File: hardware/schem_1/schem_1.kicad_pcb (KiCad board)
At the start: 4 copper layers, 69.9 x 34 mm, 87 parts, among them J1 OV7670_Conn_01x24_MountingPin, J2 Micro_SD_Card, J3 FRONT_PCB_CONNECTOR, J4 BG300-04-X-X-A_REVC, J5 UJ2-MBH-1-SMT, J6 BACK_PCB_CONNECTOR, Q1 NDS332P, SW1 BTN_BOOT, SW2 ESP32_RESET, SW4 DOWN, SW5 UP, SW6 OK, U1 ESP32-WROVER-E-JC, U2 XC6210B332MR, U5 XC6206-2.8V, U6 XC6206-1.2V, U7 128x32_OLED_SSD1306, U8 MCP23017_SO

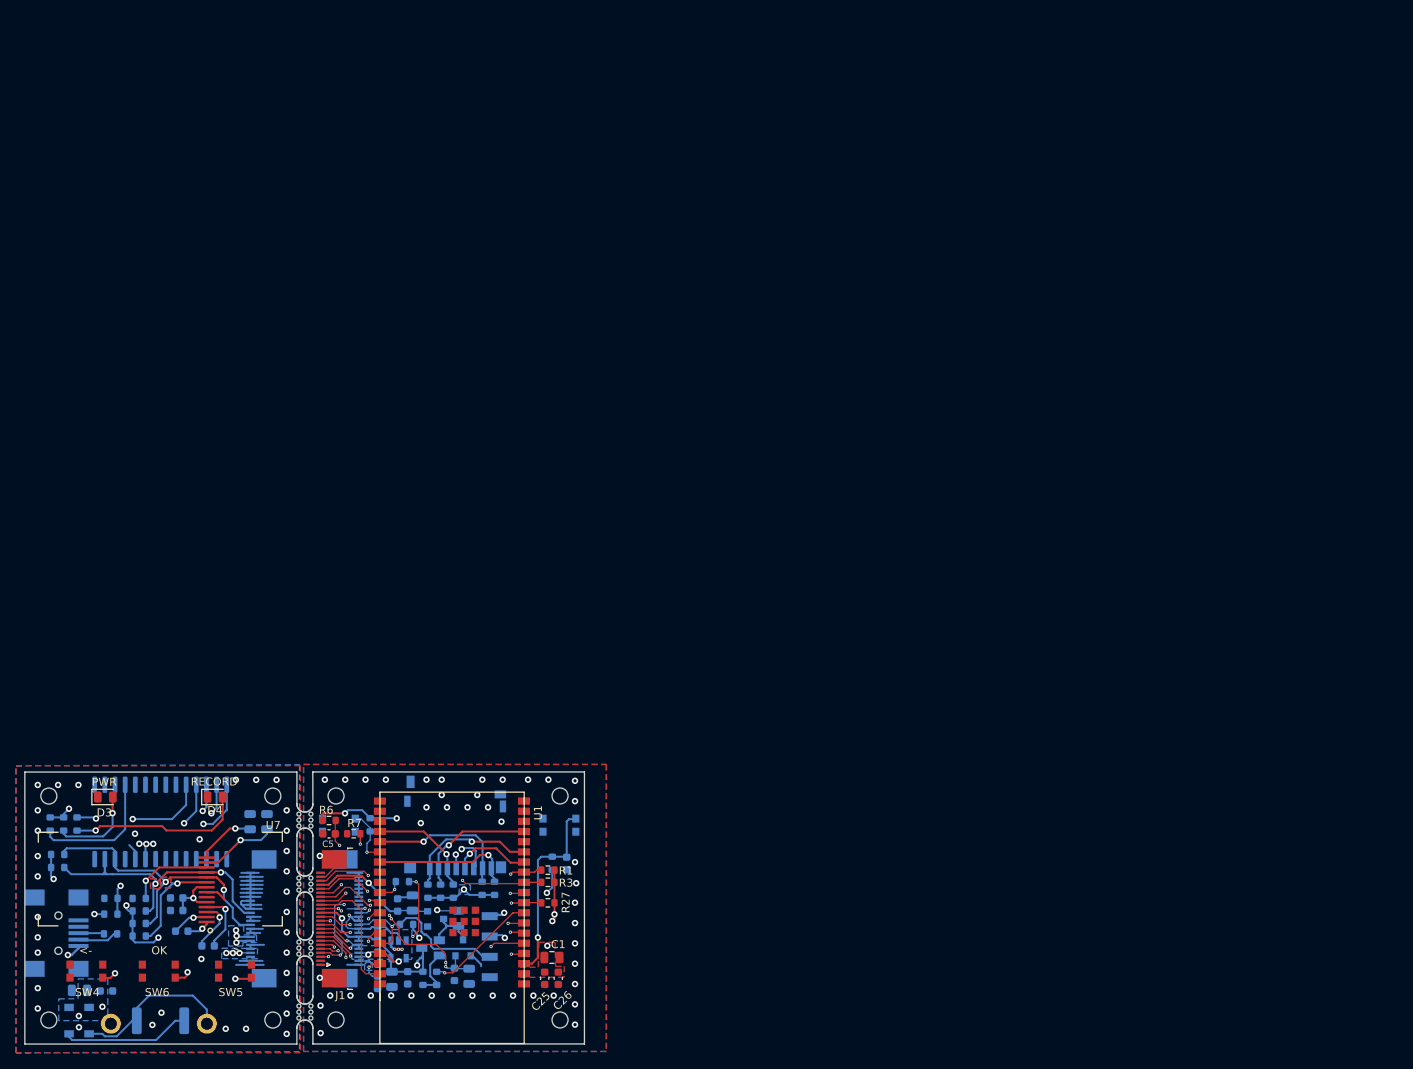
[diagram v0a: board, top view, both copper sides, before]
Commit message: move old production stuff to new folder. start pcb spin 2: add test points (smd and pads). add third diode as currently disconnected USB can not be detected. increase LED resistor values are too bright. improve OLED footprint (to accomodate inaccuracies in drawing).
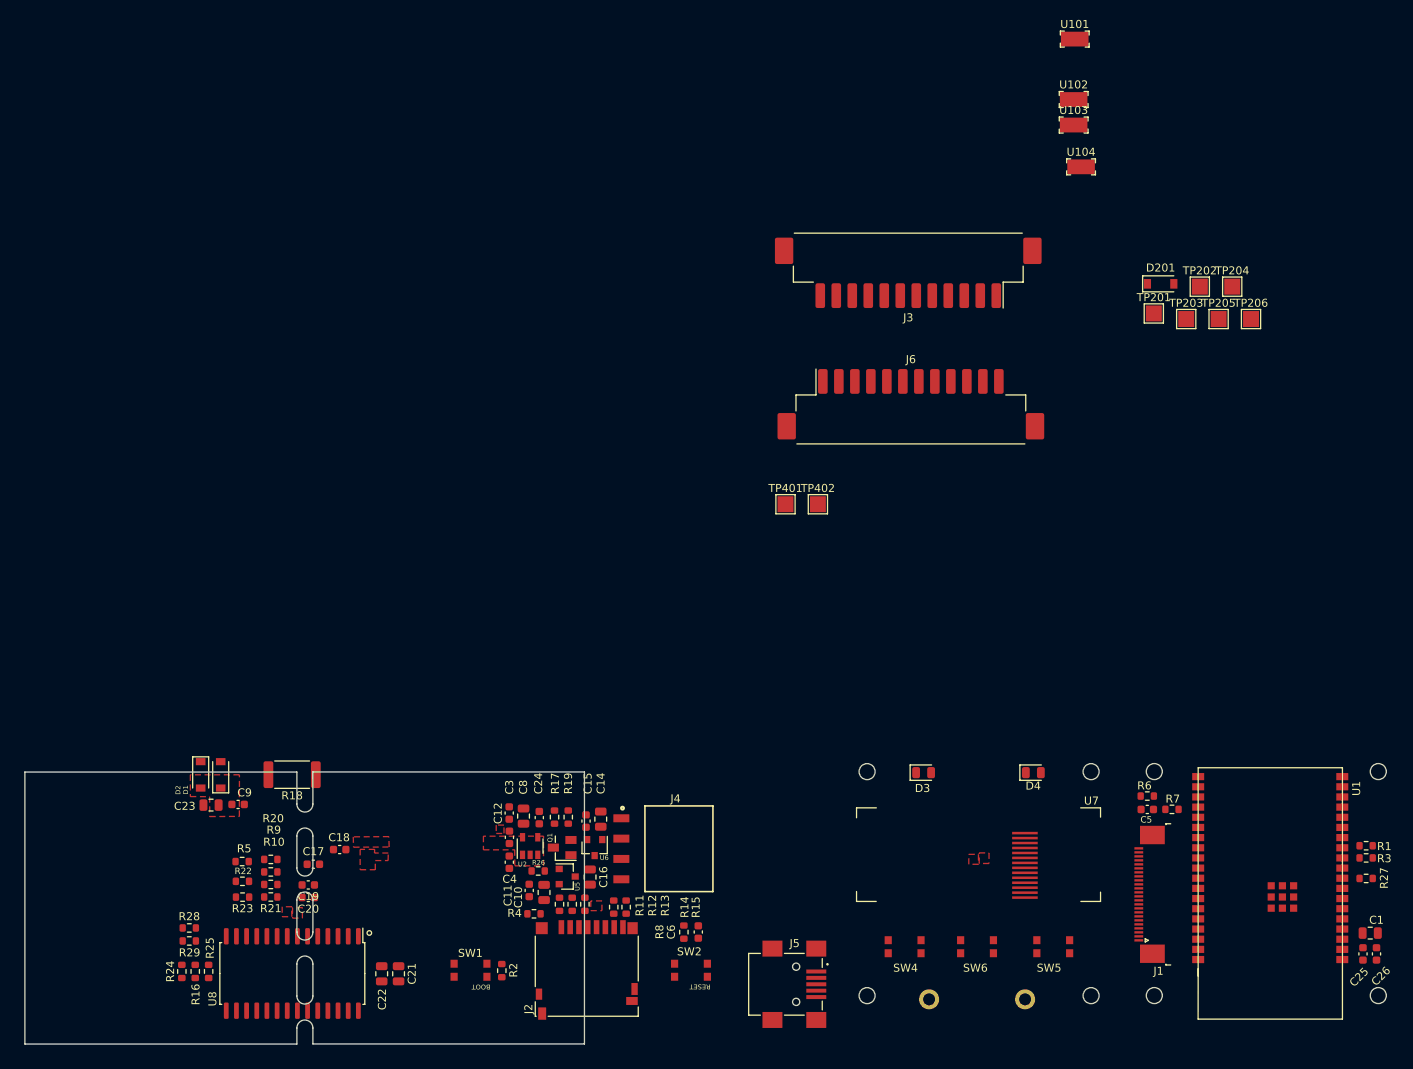
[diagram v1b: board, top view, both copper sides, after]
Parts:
- removed mouse-bite-2mm-slot (x4): VAL**, Panelization:mouse-bite-2mm-slot
- added D201: PMEG2005EGWX, Diode_SMD:D_SOD-123, F.Cu at (199.9, -64.6)
- added TP201: TestPoint, TestPoint:TestPoint_Pad_2.0x2.0mm, F.Cu at (199.1, -60.9)
- added TP202: TestPoint, TestPoint:TestPoint_Pad_2.0x2.0mm, F.Cu at (204.8, -64.2)
- added TP203: TestPoint, TestPoint:TestPoint_Pad_2.0x2.0mm, F.Cu at (203.1, -60.2)
- added TP204: TestPoint, TestPoint:TestPoint_Pad_2.0x2.0mm, F.Cu at (208.9, -64.2)
- added TP205: TestPoint, TestPoint:TestPoint_Pad_2.0x2.0mm, F.Cu at (207.2, -60.2)
- added TP206: TestPoint, TestPoint:TestPoint_Pad_2.0x2.0mm, F.Cu at (211.2, -60.2)
- added TP401: TestPoint, TestPoint:TestPoint_Pad_2.0x2.0mm, F.Cu at (153.0, -37.0)
- added TP402: TestPoint, TestPoint:TestPoint_Pad_2.0x2.0mm, F.Cu at (157.1, -37.0)
- added U101: 0805_TEST_POINT, Digikey:PC_TEST_POINT_SMD, F.Cu at (189.2, -95.2)
- added U102: 0805_TEST_POINT, Digikey:PC_TEST_POINT_SMD, F.Cu at (189.1, -87.6)
- added U103: 0805_TEST_POINT, Digikey:PC_TEST_POINT_SMD, F.Cu at (189.1, -84.4)
- added U104: 0805_TEST_POINT, Digikey:PC_TEST_POINT_SMD, F.Cu at (190.0, -79.2)
- C10, C11, C12, C14, C15, C16, C17, C18, C19, C20, C21, C22, C23, C24, C3, C4, C6, C8, C9, D1, D2, J2, J4, J5, Q1, R10, R11, R12, R13, R14, R15, R17, R18, R19, R2, R20, R21, R22, R23, R24, R26, R28, R29, R4, R5, R8, R9, SW1, SW2, U2, U5, U6, U8: moved to F.Cu
- J3: value FRONT_PCB_CONNECTOR -> Front_PCB_Connector; footprint Connector_FFC-FPC:TE_2-1734839-4_1x24-1MP_P0.5mm_Horizontal -> Connector_Hirose:Hirose_DF3EA-12P-2H_1x12-1MP_P2.00mm_Horizontal; moved to F.Cu
- J6: footprint Connector_FFC-FPC:TE_2-1734839-4_1x24-1MP_P0.5mm_Horizontal -> Connector_Hirose:Hirose_DF3EA-12P-2H_1x12-1MP_P2.00mm_Horizontal; moved to F.Cu
- R16: value 130 -> 470; moved to F.Cu
- R25: value 220 -> 470; moved to F.Cu
- moved J3 106.9 mm to (168.4, -65.9), turned to 180 degrees
- moved J6 103.6 mm to (168.7, -49.5), turned to 0 degrees
- moved C26 102.3 mm to (226.9, 19.2)
- moved C5 102.3 mm to (198.3, 1.13)
- moved C25 102.3 mm to (225.2, 19.2)
- moved D3 102.3 mm to (170.3, -3.47)
- moved D4 102.3 mm to (184.0, -3.47)
- moved H1 102.3 mm to (199.1, 24.4)
- moved H2 102.3 mm to (227.1, 24.4)
- moved H3 102.3 mm to (227.1, -3.60)
- moved H4 102.3 mm to (199.1, -3.60)
- moved R27 102.3 mm to (225.6, 9.76)
- moved R3 102.3 mm to (225.6, 7.19)
- moved R6 102.3 mm to (198.3, -0.54)
- moved R7 102.3 mm to (201.4, 1.12)
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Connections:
- C12 pad 1: /5V_USB_SC -> Net-(C12-Pad1)
- D1 pad 1: /5V_USB_SC -> Net-(C12-Pad1)
- J3 pad 10: GND -> /5V_USB_SC
- J3 pad 11: /SCL -> /5V_USB_SC
- J3 pad 2: GND -> /SDA
- J3 pad 3: /5V_USB_SC -> GND
- J3 pad 4: /5V_USB_SC -> /SCL
- J6 pad 2: GND -> /5V_USB_SC
- J6 pad 3: GND -> /5V_USB_SC
- J6 pad 5: GND -> +3V3
- J6 pad 6: GND -> +3V3
- J6 pad 9: GND -> /SCL
- U2 pad 1: /5V_USB_SC -> Net-(C12-Pad1)
- U2 pad 3: /5V_USB_SC -> Net-(C12-Pad1)
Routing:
- net GND: track 99.0 -> 0.00 mm, vias 85 -> 0
- net +3V3: track 88.8 -> 0.00 mm, vias 22 -> 0
- net /SCL: track 61.8 -> 0.00 mm, vias 3 -> 0
- net /SDA: track 60.5 -> 0.00 mm, vias 4 -> 0
- net /TWI_SCK: track 30.2 -> 0.00 mm, vias 2 -> 0
- net /GPIO Expander/BTN_DOWN: track 30.1 -> 0.00 mm, vias 2 -> 0
- net /5V_USB_SC: track 29.8 -> 0.00 mm, vias 12 -> 0
- net /CSI_D4: track 29.1 -> 0.00 mm, vias 2 -> 0
- net /TWI_SDA: track 28.8 -> 0.00 mm, vias 2 -> 0
- net /GPIO Expander/BTN_OK: track 28.4 -> 0.00 mm, vias 2 -> 0
- net /GPIO Expander/BTN_UP: track 27.8 -> 0.00 mm, vias 2 -> 0
- net /CSI_VSYNC: track 27.6 -> 0.00 mm, vias 2 -> 0
- net /CSI_D5: track 26.8 -> 0.00 mm, vias 2 -> 0
- net +1V2: track 26.3 -> 0.00 mm, vias 6 -> 0
- net /CSI_D7: track 26.0 -> 0.00 mm, vias 2 -> 0
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- added copper zone on F.Cu, net /5V_USB_SC
- added copper zone on In2.Cu, net /5V_USB_SC
- added copper zone on F.Cu, net /CSI_PCLK
- removed copper zone on B.Cu, net +3V3
- removed copper zone on In1.Cu, net +3V3
- removed copper zone on B.Cu, net /5V_USB_SC
- removed copper zone on In1.Cu, net /5V_USB_SC
- removed copper zone on B.Cu, net /CSI_PCLK
- removed copper zone on B.Cu, net /SCL
- removed copper zone on B.Cu, net /SDA
- removed copper zone on B.Cu, net GND
- removed copper zone on F.Cu, net GND
- removed copper zone on In1.Cu, net GND
- removed copper zone on In2.Cu, net GND

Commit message: make board on breadboard for easier debugging and fixing. will start writing f/w on this board
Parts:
- removed H5, H6, H7, H8: MountingHole, MountingHole:MountingHole_2mm
- removed J3: Front_PCB_Connector, Connector_Hirose:Hirose_DF3EA-12P-2H_1x12-1MP_P2.00mm_Horizontal
- removed J6: BACK_PCB_CONNECTOR, Connector_Hirose:Hirose_DF3EA-12P-2H_1x12-1MP_P2.00mm_Horizontal
- moved H3 225.5 mm to (4.97, 35.1)
- moved H2 223.0 mm to (4.97, 5.06)
- moved C1 171.8 mm to (55.0, 31.9), turned to 270 degrees
- moved J1 171.7 mm to (27.3, 24.2)
- moved C2 171.7 mm to (12.7, 3.23), turned to 0 degrees
- moved U1 170.6 mm to (43.8, 21.3)
- moved C5 170.6 mm to (28.1, 13.3)
- moved R1 170.6 mm to (55.4, 17.8)
- moved R27 170.6 mm to (55.4, 21.9)
- moved R3 170.6 mm to (55.4, 19.4)
- moved R6 170.6 mm to (28.1, 11.6)
- moved R7 170.6 mm to (31.2, 13.3)
- moved C25 168.7 mm to (57.0, 31.7)
- moved C26 168.6 mm to (58.8, 31.7)
- moved J5 149.4 mm to (7.58, 17.2)
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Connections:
- C2 pad 2: GND -> Net-(C2-Pad2)
- D1 pad 2: Net-(C2-Pad1) -> Net-(C201-Pad1)
- R18 pad 2: Net-(C2-Pad1) -> Net-(C201-Pad1)
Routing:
- removed copper zone on F.Cu, net +3V3
- removed copper zone on F.Cu, net /5V_USB_SC
- removed copper zone on In2.Cu, net /5V_USB_SC
- removed copper zone on F.Cu, net /CSI_PCLK
- removed copper zone on F.Cu, net /SCL
- removed copper zone on F.Cu, net /SDA
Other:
- board size 69.9 x 34 mm -> 80 x 40 mm
- net class 5V: via_drill 0.4 -> 0.45
- net class Default: via_drill 0.4 -> 0.45
- rule via_min_size: 0.4 -> 0.45
- board text removed: "Back PCB (with LCD) Contains the following: - OLED SCREEN - USB 5V IN - SUPERCAPACITOR + CHARGE CIRCUIT - I2C IO EXPANDER - 3 BUTTONS - LED (RECORDING) - LED (POWER)"
- board text removed: "F.CU : Signal In1.Cu : Power In2.Cu: Signal B.Cu : Signal"
- board text removed: "Front PCB (with Camera) Contains the following: - ESP32 WROVER - OV7670 CAMERA MODULE - BOOT/RESET SWITCHES FOR ESP32 - 3V3 LDO - 2.8V LDO - 1.2V LDO - SD CARD - UART CONNECTOR"
- board text removed: "Top side"
